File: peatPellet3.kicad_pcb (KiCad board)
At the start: 2 copper layers, 63 parts, among them J1 Barrel_Jack_Switch, J2 AudioJack2, J3 AudioJack2, K1 Relay_DPDT, SW1 SW_SPDT, SW2 SW_SPDT, SW3 SW_SPDT_MSM, U1 TL072, U2 L78L05_SO8, U3 LM555xM

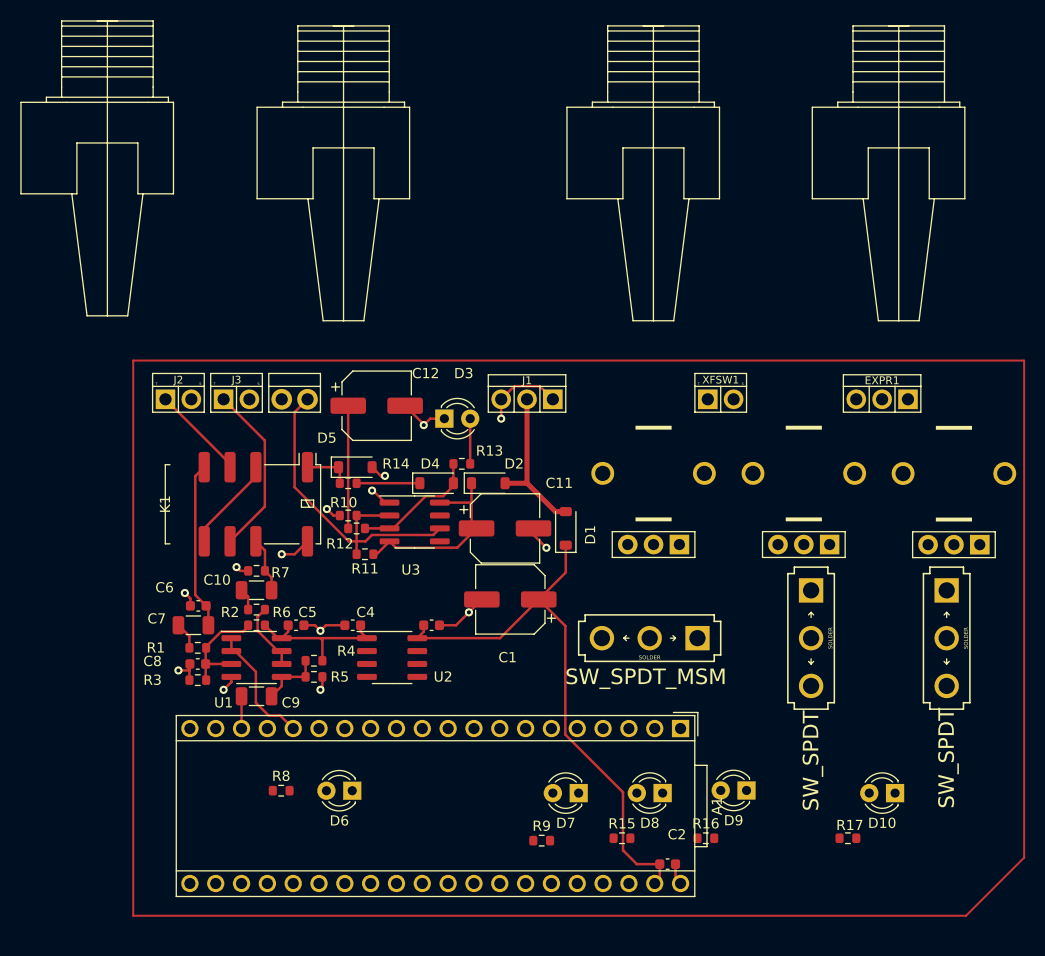
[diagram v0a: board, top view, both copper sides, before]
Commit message: finished wiring added pours
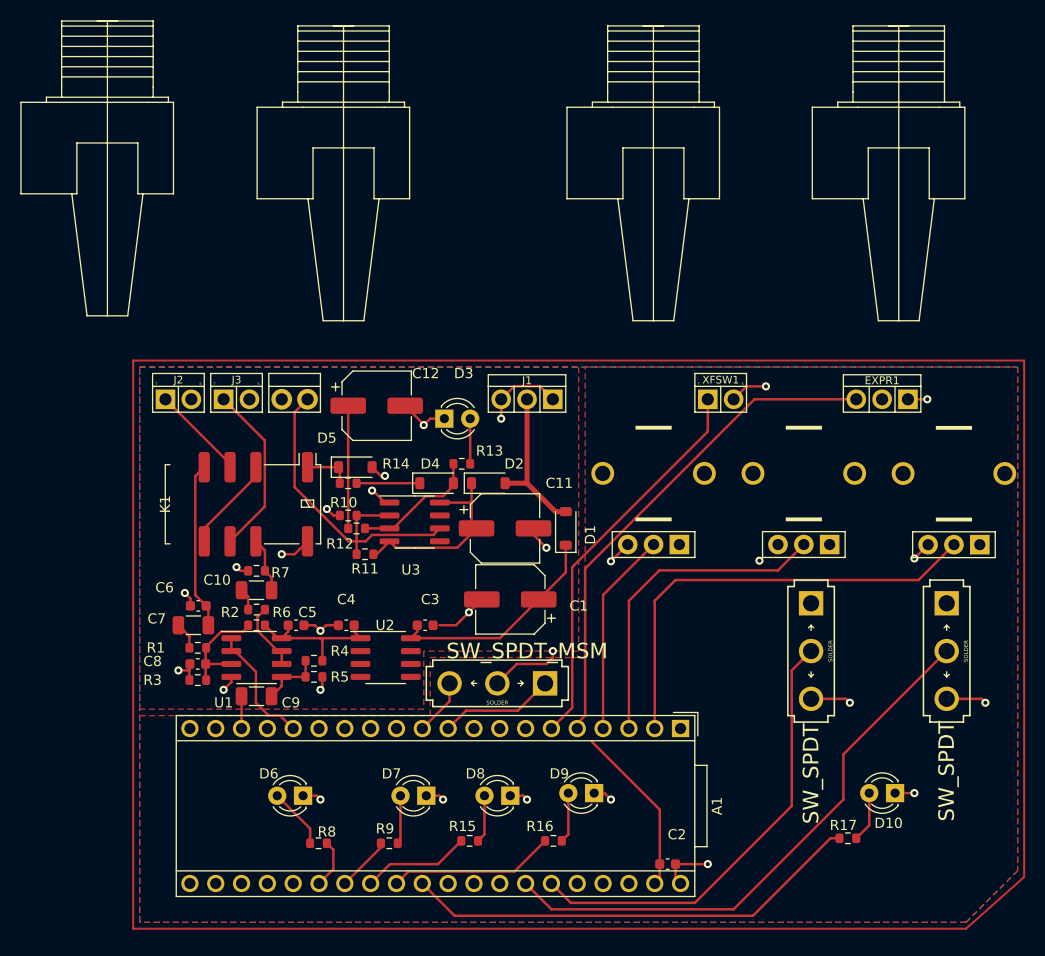
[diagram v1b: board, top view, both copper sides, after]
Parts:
- moved SW3 15.6 mm to (118.4, 118.1)
- moved D8 15.0 mm to (119.6, 129.2)
- moved D9 15.0 mm to (127.9, 128.9)
- moved R15 15.0 mm to (115.6, 133.6)
- moved R16 15.0 mm to (123.9, 133.6)
- moved D7 15.0 mm to (111.4, 129.2)
- moved R9 15.0 mm to (107.7, 133.8)
- moved R8 6.34 mm to (100.8, 133.8), turned to 180 degrees
- moved D6 4.87 mm to (99.3, 129.2)
- moved SW1 1.27 mm to (162.6, 114.9)
- moved SW2 1.27 mm to (149.2, 114.9)
- moved C3 0.64 mm to (111.3, 112.4)
- moved C4 0.64 mm to (103.5, 112.4)
- moved U2 0.64 mm to (107.4, 115.6)
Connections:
- A1 pad 10: SW4 -> SW3
- A1 pad 11: SW3 -> SW4
- A1 pad 2: unconnected-(A1-SD_DATA_3-Pad2) -> KNOB3
- A1 pad 22: KNOB1 -> unconnected-(A1-ADC_0-Pad22)
- A1 pad 23: KNOB2 -> unconnected-(A1-ADC_1-Pad23)
- A1 pad 24: KNOB3 -> unconnected-(A1-ADC_2-Pad24)
- A1 pad 25: EXP -> unconnected-(A1-ADC_3-Pad25)
- A1 pad 3: unconnected-(A1-SD_DATA_2-Pad3) -> KNOB2
- A1 pad 32: SW1 -> unconnected-(A1-SAI2_SD_B-Pad32)
- A1 pad 33: SW2 -> unconnected-(A1-SAI2_SD_A-Pad33)
- A1 pad 34: unconnected-(A1-SAI2_FS-Pad34) -> SW1
- A1 pad 35: unconnected-(A1-SAI2_SCK-Pad35) -> SW2
- A1 pad 4: unconnected-(A1-SD_DATA_1-Pad4) -> KNOB1
- A1 pad 5: unconnected-(A1-SD_DATA_0-Pad5) -> EXP
- A1 pad 6: unconnected-(A1-SD_CMD-Pad6) -> XFS
- A1 pad 9: XFS -> unconnected-(A1-SPI1_SCK-Pad9)
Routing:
- net SW1: track 0.00 -> 55.6 mm
- net EXP: track 0.00 -> 49.6 mm
- net LED5: track 0.00 -> 45.5 mm
- net SW2: track 0.00 -> 44.4 mm
- net KNOB3: track 0.00 -> 44.3 mm
- net XFS: track 0.00 -> 38.8 mm
- net GND: track 44.3 -> 81.3 mm, vias 14 -> 28
- net KNOB2: track 0.00 -> 32.1 mm
- net KNOB1: track 0.00 -> 20.2 mm
- net +9V: track 75.4 -> 58.6 mm
- net LED4: track 0.00 -> 16.3 mm
- net SW3: track 0.00 -> 11.4 mm
- net LED3: track 0.00 -> 10.6 mm
- net Net-(D6-A): track 0.00 -> 6.01 mm
- net SW4: track 0.00 -> 5.56 mm
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- added copper zone on F.Cu, net +3.3VA
- added copper zone on F.Cu, net +9V
- added copper zone on B.Cu, net GND

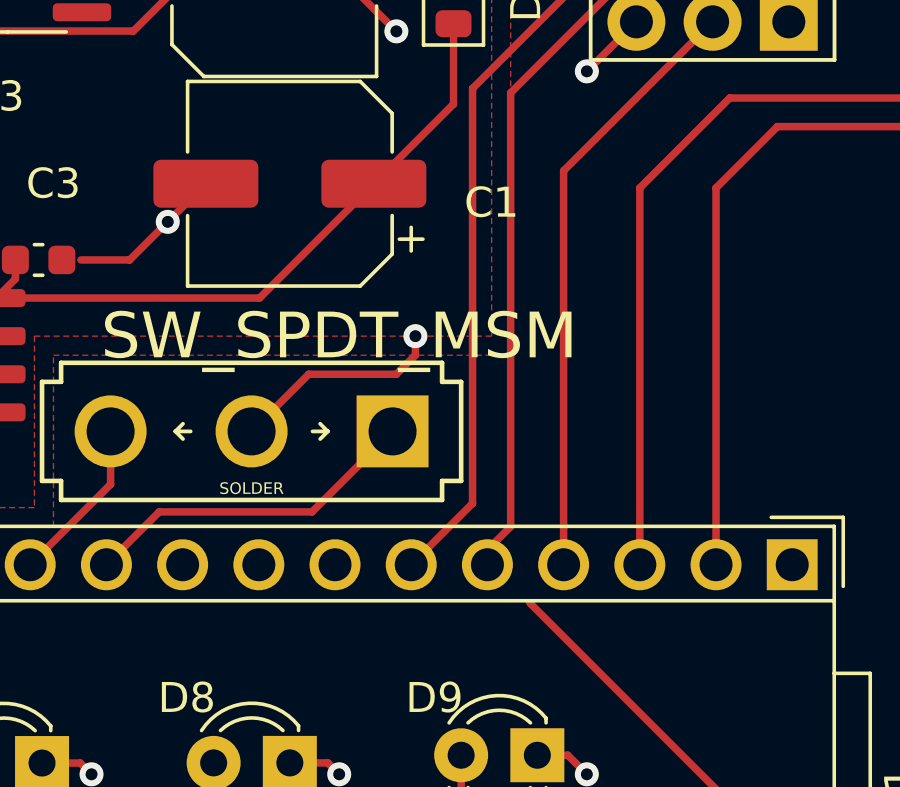
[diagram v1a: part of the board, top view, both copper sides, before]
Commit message: seed power and 3.3v pour update
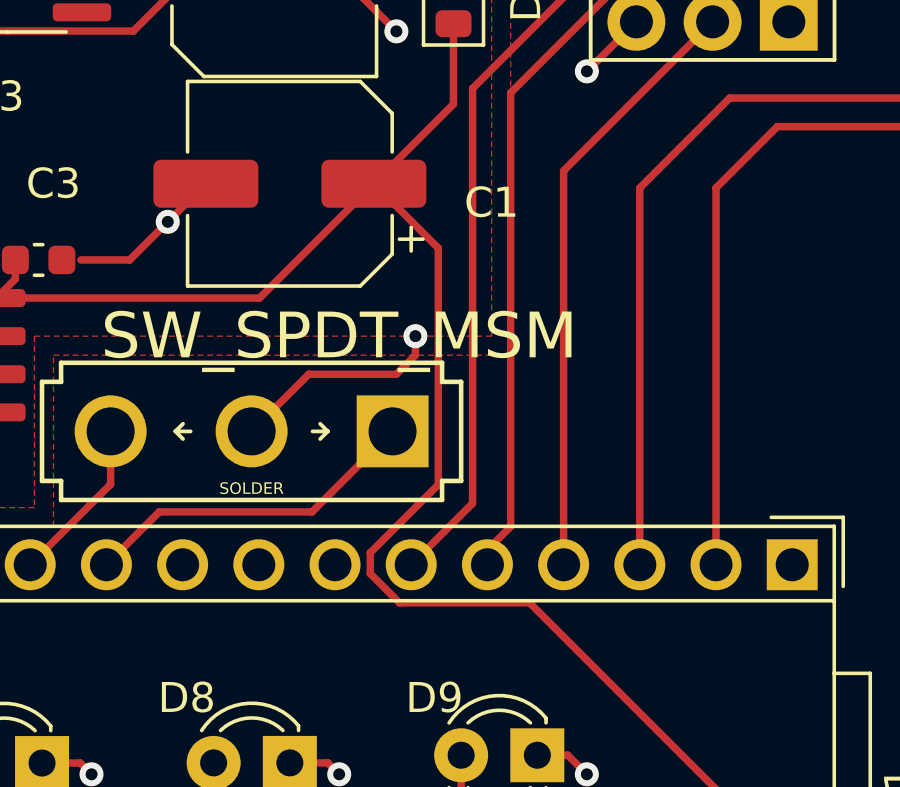
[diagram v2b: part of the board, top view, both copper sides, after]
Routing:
- net +9V: track 58.6 -> 79.1 mm
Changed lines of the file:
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@@
   (segment (start 112.71 100.33) (end 115.825 100.33) (width 0.25) (layer "F.Cu") (net 66))
   (segment (start 115.825 100.33) (end 115.825 102.375) (width 0.25) (layer "F.Cu") (net 66))
+  (segment (start 124.588 119.887) (end 122.32 122.155) (width 0.25) (layer "F.Cu") (net 66))
   (segment (start 110.49 113.03) (end 109.855 113.665) (width 0.25) (layer "F.Cu") (net 66))
   (segment (start 109.855 113.665) (end 118.63 113.665) (width 0.25) (layer "F.Cu") (net 66))
@@
   (segment (start 115.825 102.375) (end 116.32 102.87) (width 0.25) (layer "F.Cu") (net 66))
   (segment (start 134.34 130.53) (end 127.635 123.825) (width 0.25) (layer "F.Cu") (net 66))
+  (segment (start 122.32 122.155) (end 122.32 122.851701) (width 0.25) (layer "F.Cu") (net 66))
   (segment (start 110.49 112.395) (end 110.49 113.03) (width 0.25) (layer "F.Cu") (net 66))
+  (segment (start 124.588 112.003) (end 124.588 119.887) (width 0.25) (layer "F.Cu") (net 66))
   (segment (start 134.34 135.89) (end 134.34 130.53) (width 0.25) (layer "F.Cu") (net 66))
   (segment (start 108.385 104.765) (end 107.76 104.14) (width 0.25) (layer "F.Cu") (net 66))
   (segment (start 116.32 102.87) (end 114.425 104.765) (width 0.25) (layer "F.Cu") (net 66))
   (segment (start 106.17 105.41) (end 106.49 105.41) (width 0.25) (layer "F.Cu") (net 66))
+  (segment (start 122.44 109.855) (end 124.588 112.003) (width 0.25) (layer "F.Cu") (net 66))
   (segment (start 118.63 113.665) (end 122.44 109.855) (width 0.25) (layer "F.Cu") (net 66))
   (segment (start 115.825 98.425) (end 115.825 100.33) (width 0.25) (layer "F.Cu") (net 66))
+  (segment (start 122.32 122.851701) (end 123.293299 123.825) (width 0.25) (layer "F.Cu") (net 66))
   (segment (start 134.34 137.3) (end 133.845 137.795) (width 0.25) (layer "F.Cu") (net 66))
   (segment (start 106.49 105.41) (end 107.76 104.14) (width 0.25) (layer "F.Cu") (net 66))
+  (segment (start 123.293299 123.825) (end 127.635 123.825) (width 0.25) (layer "F.Cu") (net 66))
   (segment (start 134.34 135.89) (end 134.34 137.3) (width 0.25) (layer "F.Cu") (net 66))
   (zone (net 66) (net_name "+9V") (layer "F.Cu") (hatch edge 0.5)

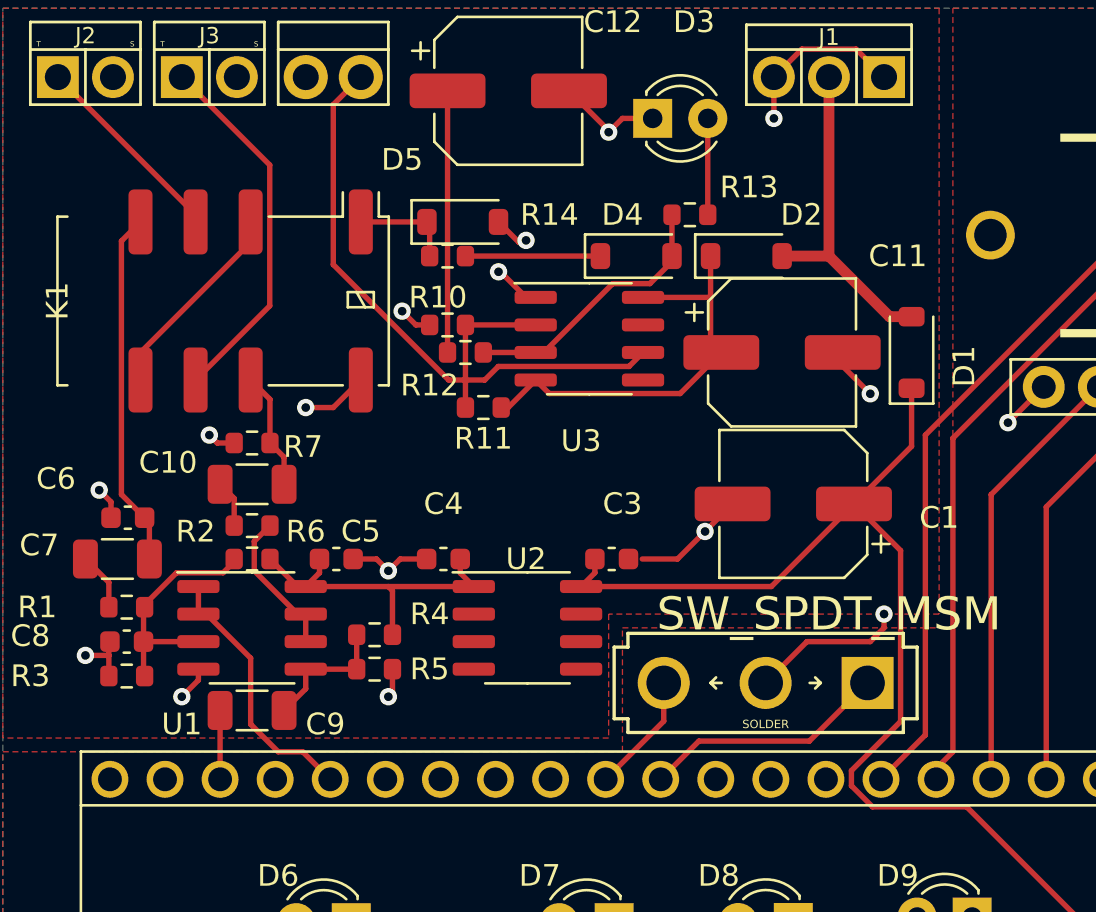
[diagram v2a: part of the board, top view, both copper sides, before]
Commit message: fixed courtyard overlaps
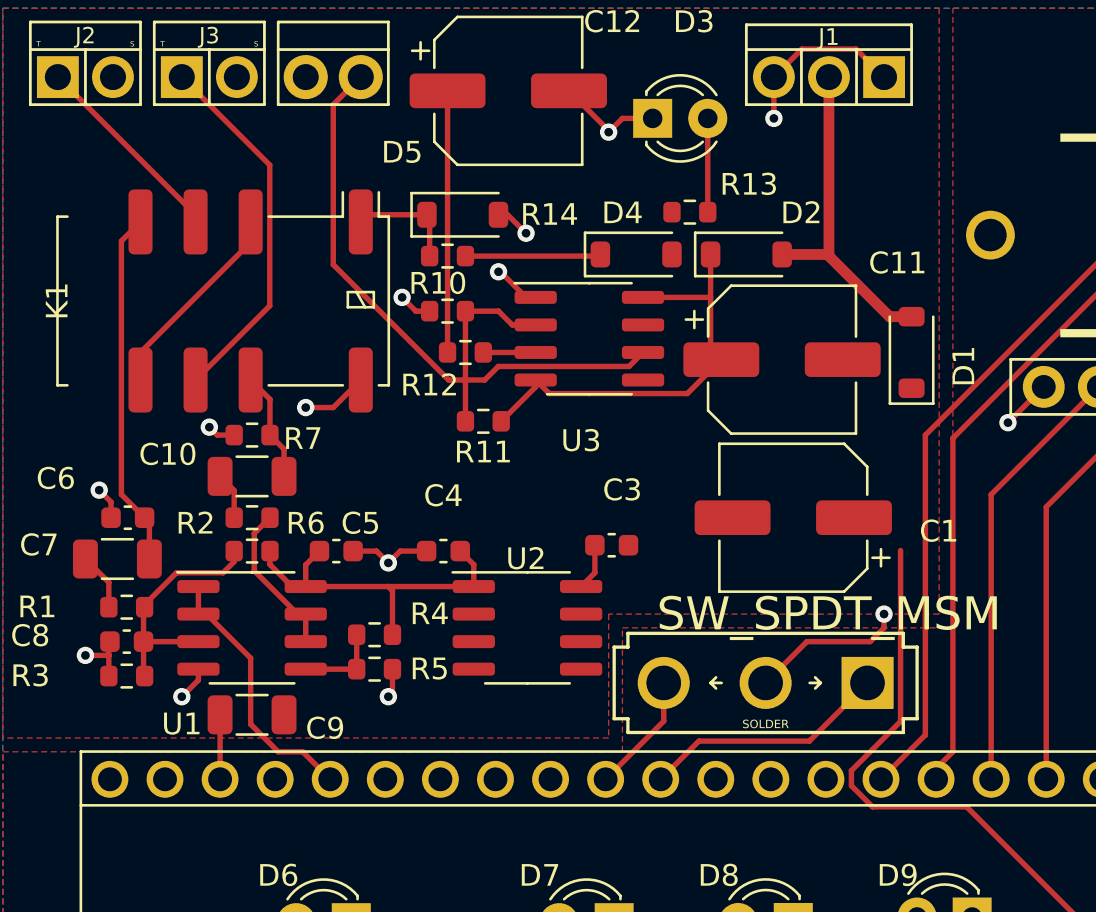
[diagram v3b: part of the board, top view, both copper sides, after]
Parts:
- moved R11 0.64 mm to (105.3, 106.0)
- moved C1 0.63 mm to (119.6, 110.5)
- moved C3 0.63 mm to (111.3, 111.8)
- moved R10 0.63 mm to (103.7, 101.0)
- moved C10 0.37 mm to (94.7, 108.6)
- moved R6 0.37 mm to (94.7, 110.5)
- moved C4 0.36 mm to (103.5, 112.0)
- moved C5 0.36 mm to (98.6, 112.0)
- moved R2 0.36 mm to (94.7, 112.0)
- moved R7 0.36 mm to (94.7, 106.7)
- moved C11 0.33 mm to (119.1, 103.2)
- moved D5 0.33 mm to (104.4, 96.5)
- moved C9 0.20 mm to (94.7, 119.6)
- moved R13 0.12 mm to (114.9, 96.4)
- moved D2 0.08 mm to (117.5, 98.3)
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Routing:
- net +9V: track 79.1 -> 56.8 mm
- net Net-(D4-A): track 12.6 -> 3.05 mm
- net GND: track 81.3 -> 73.5 mm, vias 28 -> 26
- net Net-(U1B-+): track 6.26 -> 3.94 mm
- net Net-(U3-THR): track 33.2 -> 34.8 mm
- net +5V: track 15.4 -> 16.5 mm

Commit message: DRC first run through
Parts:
- moved ? 6.35 mm to (69.8, 130.7)
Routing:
- net GND: track 73.5 -> 75.8 mm
- net Net-(D4-A): track 3.05 -> 4.36 mm
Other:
- board outline added: 87.6 x 55.9 mm
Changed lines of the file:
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@@
         (effects (font (size 1 1) (thickness 0.15)))
     )
-    (fp_text value "Electrosmith_Daisy_Seed_Rev4" (at 6.985 54.145) (layer "F.Fab")
+    (fp_text value "Electrosmith_Daisy_Seed_Rev4" (at 1.905 37.96) (layer "F.Fab")
         (effects (font (size 1 1) (thickness 0.15)))
     )
@@
   )
   (footprint "enclosures:MOMENTARY" (layer "F.Cu")
-    (at 76.2 130.712501 -90)
+    (at 69.85 130.712501 -90)
     (attr through_hole)
     (fp_text reference "" (at 0 0 -270) (layer "F.SilkS")
@@
       (xy 170.18 86.36)
     )
-    (stroke (width 0.2) (type solid)) (fill none) (layer "F.Cu"))
+    (stroke (width 0.2) (type solid)) (fill none) (layer "Edge.Cuts"))
   (segment (start 113.525 122.555) (end 115.287676 120.792324) (width 0.25) (layer "F.Cu") (net 6))
   (segment (start 115.287676 120.792324) (end 120.380676 120.792324) (width 0.25) (layer "F.Cu") (net 6))
@@
   (segment (start 88.175 110.49) (end 88.175 109.765) (width 0.25) (layer "F.Cu") (net 17))
   (segment (start 120.904 129.16) (end 121.284 129.54) (width 0.25) (layer "F.Cu") (net 17))
+  (segment (start 144.3825 106.045) (end 145.97 104.4575) (width 0.25) (layer "F.Cu") (net 17))
   (segment (start 118.745 90.17) (end 118.745 92.075) (width 0.25) (layer "F.Cu") (net 17))
   (segment (start 88.075 117.7925) (end 88.075 116.84) (width 0.25) (layer "F.Cu") (net 17))
@@
   (segment (start 118.745 90.17) (end 120.0352 88.8798) (width 0.25) (layer "F.Cu") (net 17))
   (segment (start 158.75 90.17) (end 160.655 90.17) (width 0.25) (layer "F.Cu") (net 17))
-  (segment (start 159.385 106.045) (end 159.385 105.8225) (width 0.25) (layer "F.Cu") (net 17))
   (segment (start 106.045 96.52) (end 106.4645 96.52) (width 0.25) (layer "F.Cu") (net 17))
   (segment (start 98.425 105.41) (end 97.155 105.41) (width 0.25) (layer "F.Cu") (net 17))
@@
   (segment (start 111.379 129.164972) (end 112.653972 129.164972) (width 0.25) (layer "F.Cu") (net 17))
   (segment (start 129.54 106.1085) (end 131.191 104.4575) (width 0.25) (layer "F.Cu") (net 17))
+  (segment (start 144.145 106.045) (end 144.3825 106.045) (width 0.25) (layer "F.Cu") (net 17))
   (segment (start 120.0352 88.8798) (end 122.5348 88.8798) (width 0.25) (layer "F.Cu") (net 17))
   (segment (start 127.889 128.905) (end 128.904 128.905) (width 0.25) (layer "F.Cu") (net 17))
@@
   (segment (start 121.21 98.35) (end 121.285 98.425) (width 0.25) (layer "F.Cu") (net 35))
   (segment (start 104.52 98.425) (end 110.745 98.425) (width 0.25) (layer "F.Cu") (net 36))
-  (segment (start 114.045 98.68) (end 114.045 98.425) (width 0.25) (layer "F.Cu") (net 37))
+  (segment (start 114.045 98.35) (end 114.045 96.4) (width 0.25) (layer "F.Cu") (net 37))
   (segment (start 107.76 102.87) (end 105.345 102.87) (width 0.25) (layer "F.Cu") (net 37))
-  (segment (start 107.76 102.87) (end 108.136751 102.87) (width 0.25) (layer "F.Cu") (net 37))
   (segment (start 102.87 96.975) (end 102.745 96.85) (width 0.25) (layer "F.Cu") (net 38))
   (segment (start 102.745 96.52) (end 99.695 96.52) (width 0.25) (layer "F.Cu") (net 38))
